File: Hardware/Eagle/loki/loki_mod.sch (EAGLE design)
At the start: 39 parts

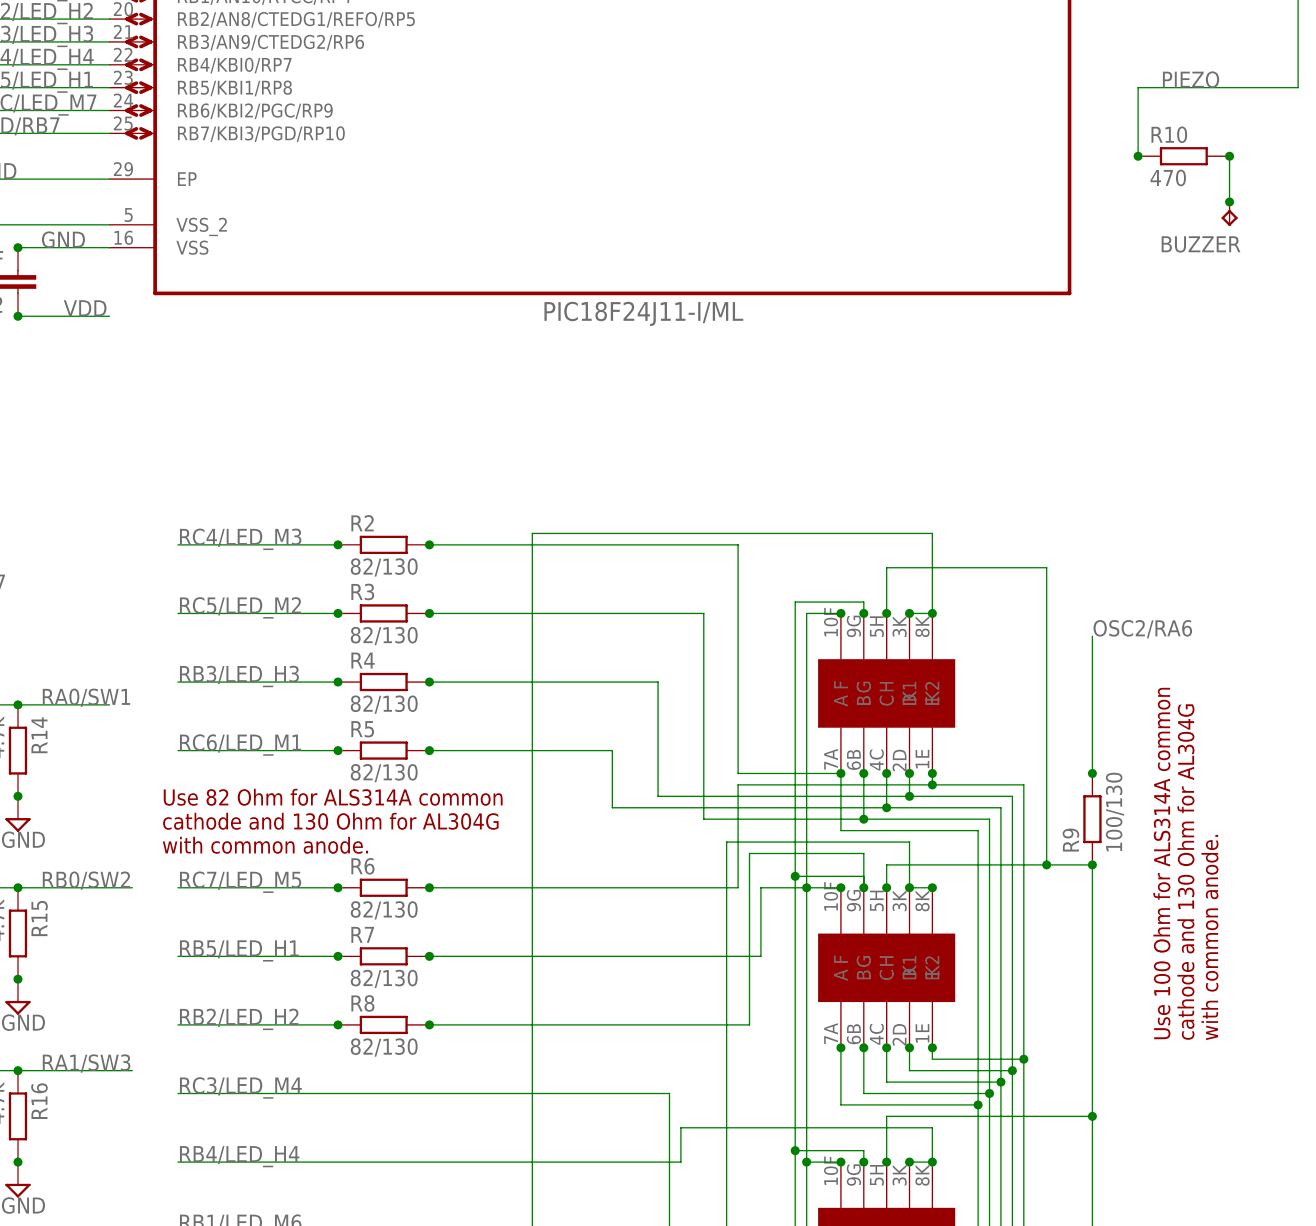
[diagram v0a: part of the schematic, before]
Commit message: Lowered resistor values a bit.
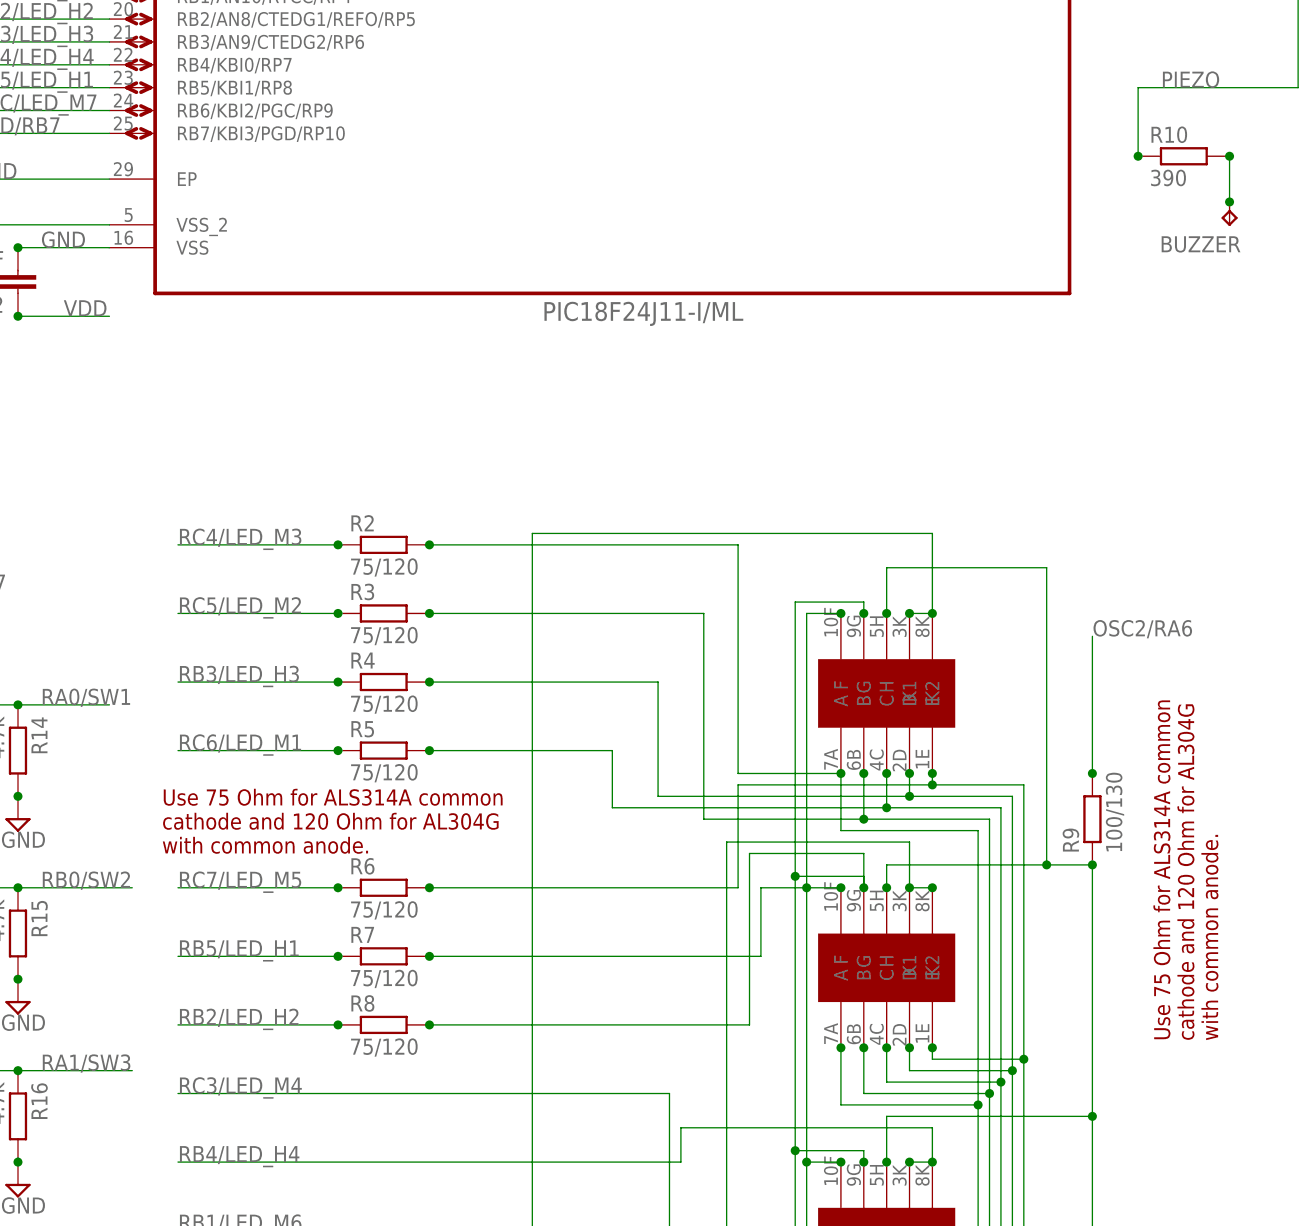
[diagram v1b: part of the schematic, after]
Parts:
- R10: value 470 -> 390
- R2, R3, R4, R5, R6, R7, R8: value 82/130 -> 75/120
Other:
- note added: "Use 75 Ohm for ALS314A common cathode and 120 Ohm for AL304G with common anode."
- note removed: "Use 100 Ohm for ALS314A common cathode and 130 Ohm for AL304G with common anode."
- note removed: "Use 82 Ohm for ALS314A common cathode and 130 Ohm for AL304G with common anode."
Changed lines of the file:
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@@
 <part name="SUPPLY2" library="supply2" deviceset="GND" device=""/>
 <part name="SUPPLY3" library="supply2" deviceset="GND" device=""/>
-<part name="R2" library="resistor" deviceset="R-EU_" device="R0402" value="82/130"/>
-<part name="R3" library="resistor" deviceset="R-EU_" device="R0402" value="82/130"/>
-<part name="R4" library="resistor" deviceset="R-EU_" device="R0402" value="82/130"/>
-<part name="R5" library="resistor" deviceset="R-EU_" device="R0402" value="82/130"/>
-<part name="R6" library="resistor" deviceset="R-EU_" device="R0402" value="82/130"/>
-<part name="R7" library="resistor" deviceset="R-EU_" device="R0402" value="82/130"/>
-<part name="R8" library="resistor" deviceset="R-EU_" device="R0402" value="82/130"/>
+<part name="R2" library="resistor" deviceset="R-EU_" device="R0402" value="75/120"/>
+<part name="R3" library="resistor" deviceset="R-EU_" device="R0402" value="75/120"/>
+<part name="R4" library="resistor" deviceset="R-EU_" device="R0402" value="75/120"/>
+<part name="R5" library="resistor" deviceset="R-EU_" device="R0402" value="75/120"/>
+<part name="R6" library="resistor" deviceset="R-EU_" device="R0402" value="75/120"/>
+<part name="R7" library="resistor" deviceset="R-EU_" device="R0402" value="75/120"/>
+<part name="R8" library="resistor" deviceset="R-EU_" device="R0402" value="75/120"/>
 <part name="R14" library="resistor" deviceset="R-EU_" device="R0402" value="4.7k"/>
 <part name="R15" library="resistor" deviceset="R-EU_" device="R0402" value="4.7k"/>
@@
 <part name="1M" library="l104g" deviceset="L104G" device=""/>
 <part name="R9" library="resistor" deviceset="R-EU_" device="R0402" value="100/130"/>
-<part name="R10" library="resistor" deviceset="R-EU_" device="R0402" value="470"/>
+<part name="R10" library="resistor" deviceset="R-EU_" device="R0402" value="390"/>
 <part name="BUZZER" library="testpad" deviceset="TP" device="TP06SQ"/>
 </parts>
@@
 This is public domain.</text>
 <text x="-22.86" y="-110.49" size="2.54" layer="94" font="vector">Pulsar P3 Loki Mod</text>
-<text x="-77.978" y="-11.43" size="1.778" layer="94">Use 82 Ohm for ALS314A common
-cathode and 130 Ohm for AL304G
+<text x="-77.978" y="-11.43" size="1.778" layer="94">Use 75 Ohm for ALS314A common
+cathode and 120 Ohm for AL304G
 with common anode.</text>
-<text x="39.37" y="-32.258" size="1.778" layer="94" rot="R90">Use 100 Ohm for ALS314A common
-cathode and 130 Ohm for AL304G
+<text x="39.37" y="-32.258" size="1.778" layer="94" rot="R90">Use 75 Ohm for ALS314A common
+cathode and 120 Ohm for AL304G
 with common anode.</text>
 <text x="-118.364" y="87.122" size="1.778" layer="94">Do not use
